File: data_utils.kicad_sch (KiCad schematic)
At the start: 35 parts, among them J10 Conn_01x05, J13 OUTSIDE LED, J5 USB_C_Receptacle_USB2.0_16P, J6 Conn_01x02, J7 Conn_01x02, J8 Conn_01x02, Q4 BC817, Q5 BC817, Q6 BC817, Q7 BC817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

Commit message: near end
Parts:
- R40, R41: footprint Resistor_THT:R_Axial_DIN0309_L9.0mm_D3.2mm_P15.24mm_Horizontal -> Resistor_SMD:R_1210_3225Metric_Pad1.30x2.65mm_HandSolder
- R42: footprint Resistor_THT:R_Axial_DIN0309_L9.0mm_D3.2mm_P15.24mm_Horizontal -> Resistor_SMD:R_0603_1608Metric_Pad0.98x0.95mm_HandSolder
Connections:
- net at R50.2, U8.7 (CANH): now also J6.2 (Pin_2); no longer J6.1 (Pin_1)
- net at R50.1, U8.6 (CANL): now also J6.1 (Pin_1); no longer J6.2 (Pin_2)
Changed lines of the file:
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@@
 	(wire
 		(pts
-			(xy 215.9 121.92) (xy 215.9 129.54)
+			(xy 107.95 48.26) (xy 107.95 44.45)
 		)
 		(stroke
@@
 	(wire
 		(pts
-			(xy 205.74 116.84) (xy 205.74 120.65)
+			(xy 215.9 121.92) (xy 215.9 129.54)
 		)
 		(stroke
@@
 	(wire
 		(pts
-			(xy 107.95 48.26) (xy 107.95 44.45)
+			(xy 205.74 116.84) (xy 205.74 120.65)
 		)
 		(stroke
@@
 			)
 		)
-		(property "Footprint" "Resistor_THT:R_Axial_DIN0309_L9.0mm_D3.2mm_P15.24mm_Horizontal"
+		(property "Footprint" "Resistor_SMD:R_0603_1608Metric_Pad0.98x0.95mm_HandSolder"
 			(at 194.31 57.658 90)
 			(effects
@@
 	(symbol
 		(lib_id "Connector_Generic:Conn_01x02")
-		(at 113.03 48.26 0)
+		(at 113.03 50.8 0)
+		(mirror x)
 		(unit 1)
 		(exclude_from_sim no)
@@
 		(dnp no)
 		(property "Reference" "J6"
-			(at 115.57 48.2599 0)
+			(at 115.57 50.8001 0)
 			(effects
 				(font
@@
 		)
 		(property "Value" "Conn_01x02"
-			(at 109.22 53.848 0)
+			(at 109.22 45.212 0)
 			(effects
 				(font
@@
 		)
 		(property "Footprint" "Connector_PinSocket_2.00mm:PinSocket_1x02_P2.00mm_Horizontal"
-			(at 113.03 48.26 0)
+			(at 113.03 50.8 0)
 			(effects
 				(font
@@
 		)
 		(property "Datasheet" "~"
-			(at 113.03 48.26 0)
+			(at 113.03 50.8 0)
 			(effects
 				(font
@@
 		)
 		(property "Description" "Generic connector, single row, 01x02, script generated (kicad-library-utils/schlib/autogen/connector/)"
-			(at 113.03 48.26 0)
+			(at 113.03 50.8 0)
 			(effects
 				(font
@@
 			)
 		)
-		(property "Footprint" "Resistor_THT:R_Axial_DIN0309_L9.0mm_D3.2mm_P15.24mm_Horizontal"
+		(property "Footprint" "Resistor_SMD:R_1210_3225Metric_Pad1.30x2.65mm_HandSolder"
 			(at 177.8 46.482 90)
 			(effects
@@
 			)
 		)
-		(property "Footprint" "Resistor_THT:R_Axial_DIN0309_L9.0mm_D3.2mm_P15.24mm_Horizontal"
+		(property "Footprint" "Resistor_SMD:R_1210_3225Metric_Pad1.30x2.65mm_HandSolder"
 			(at 177.8 47.498 90)
 			(effects

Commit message: bit artık
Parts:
- R51, R52, R53, R56, R57, R58, R59: footprint Resistor_THT:R_Axial_DIN0207_L6.3mm_D2.5mm_P7.62mm_Horizontal -> Resistor_SMD:R_1210_3225Metric_Pad1.30x2.65mm_HandSolder
- R54, R72: footprint Resistor_SMD:R_0603_1608Metric_Pad0.98x0.95mm_HandSolder -> Resistor_SMD:R_1210_3225Metric_Pad1.30x2.65mm_HandSolder
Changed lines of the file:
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@@
 			)
 		)
-		(property "Footprint" "Resistor_SMD:R_0603_1608Metric_Pad0.98x0.95mm_HandSolder"
+		(property "Footprint" "Resistor_SMD:R_1210_3225Metric_Pad1.30x2.65mm_HandSolder"
 			(at 108.712 107.95 90)
 			(effects
@@
 			)
 		)
-		(property "Footprint" "Resistor_THT:R_Axial_DIN0207_L6.3mm_D2.5mm_P7.62mm_Horizontal"
+		(property "Footprint" "Resistor_SMD:R_1210_3225Metric_Pad1.30x2.65mm_HandSolder"
 			(at 161.29 113.792 90)
 			(effects
@@
 			)
 		)
-		(property "Footprint" "Resistor_THT:R_Axial_DIN0207_L6.3mm_D2.5mm_P7.62mm_Horizontal"
+		(property "Footprint" "Resistor_SMD:R_1210_3225Metric_Pad1.30x2.65mm_HandSolder"
 			(at 67.31 108.712 90)
 			(effects
@@
 			)
 		)
-		(property "Footprint" "Resistor_THT:R_Axial_DIN0207_L6.3mm_D2.5mm_P7.62mm_Horizontal"
+		(property "Footprint" "Resistor_SMD:R_1210_3225Metric_Pad1.30x2.65mm_HandSolder"
 			(at 69.342 118.11 90)
 			(effects
@@
 			)
 		)
-		(property "Footprint" "Resistor_THT:R_Axial_DIN0207_L6.3mm_D2.5mm_P7.62mm_Horizontal"
+		(property "Footprint" "Resistor_SMD:R_1210_3225Metric_Pad1.30x2.65mm_HandSolder"
 			(at 163.322 123.19 90)
 			(effects
@@
 			)
 		)
-		(property "Footprint" "Resistor_THT:R_Axial_DIN0207_L6.3mm_D2.5mm_P7.62mm_Horizontal"
+		(property "Footprint" "Resistor_SMD:R_1210_3225Metric_Pad1.30x2.65mm_HandSolder"
 			(at 102.108 118.11 90)
 			(effects
@@
 			)
 		)
-		(property "Footprint" "Resistor_THT:R_Axial_DIN0207_L6.3mm_D2.5mm_P7.62mm_Horizontal"
+		(property "Footprint" "Resistor_SMD:R_1210_3225Metric_Pad1.30x2.65mm_HandSolder"
 			(at 201.93 115.062 90)
 			(effects
@@
 			)
 		)
-		(property "Footprint" "Resistor_SMD:R_0603_1608Metric_Pad0.98x0.95mm_HandSolder"
+		(property "Footprint" "Resistor_SMD:R_1210_3225Metric_Pad1.30x2.65mm_HandSolder"
 			(at 109.22 95.758 90)
 			(effects
@@
 			)
 		)
-		(property "Footprint" "Resistor_THT:R_Axial_DIN0207_L6.3mm_D2.5mm_P7.62mm_Horizontal"
+		(property "Footprint" "Resistor_SMD:R_1210_3225Metric_Pad1.30x2.65mm_HandSolder"
 			(at 203.962 124.46 90)
 			(effects

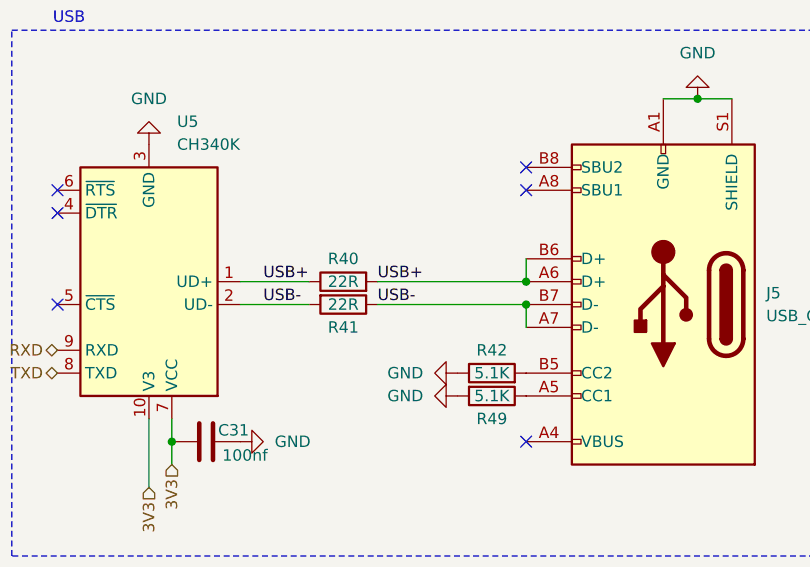
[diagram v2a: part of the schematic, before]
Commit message: esp-32 layout changes
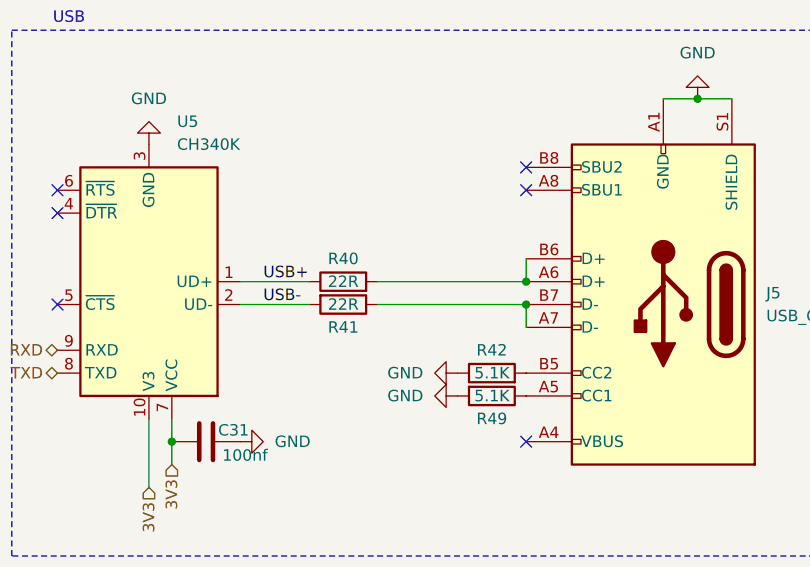
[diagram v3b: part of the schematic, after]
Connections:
- net USB+: no longer J5.A6 (D+), J5.B6 (D+), R40.2
- net USB-: no longer J5.A7 (D-), J5.B7 (D-), R41.1
- new net: J5.A7 (D-), J5.B7 (D-), R41.1
- new net: J5.A6 (D+), J5.B6 (D+), R40.2
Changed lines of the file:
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@@
-	)
-	(label "USB-"
-		(at 181.61 48.26 0)
-		(effects
-			(font
-				(size 1.27 1.27)
-			)
-			(justify left bottom)
-		)
 	)
 	(label "USB-"
@@
 		(effects
 			(font
-				(size 1.27 1.27)
-			)
-			(justify left bottom)
-		)
-	)
-	(label "USB+"
-		(at 181.61 45.72 0)
-		(effects
-			(font

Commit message: BMS DONE IHOPE
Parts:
- removed C31: 100nf, Capacitor_SMD:C_0805_2012Metric_Pad1.18x1.45mm_HandSolder, symbol Device:C
- removed J10: Conn_01x05, Connector_PinSocket_2.00mm:PinSocket_1x05_P2.00mm_Vertical, symbol Connector_Generic:Conn_01x05
- removed R40, R41: 22R, Resistor_SMD:R_1210_3225Metric_Pad1.30x2.65mm_HandSolder, symbol Device:R
- removed U5: CH340K, Package_SO:SSOP-10-1EP_3.9x4.9mm_P1mm_EP2.1x3.3mm, symbol Interface_USB:CH340K
- added J1: Conn_01x09, Connector_PinSocket_2.54mm:PinSocket_1x09_P2.54mm_Vertical, symbol Connector_Generic:Conn_01x09
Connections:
- net +5V: now also J1.9 (Pin_9)
- net GND: now also J1.1 (Pin_1)
- net PB3: now also J1.5 (Pin_5)
- net PB4: now also J1.6 (Pin_6)
- net PB5: now also J1.7 (Pin_7)
- net USB+: now also J5.A6 (D+), J5.B6 (D+)
- net USB-: now also J5.A7 (D-), J5.B7 (D-)
- net at R54.1: now also JP1.1 (A); no longer JP1.3 (B)
- net at R53.1: now also JP1.3 (B); no longer JP1.2 (C)
- net at Q7.2 (E): now also JP1.2 (C); no longer JP1.1 (A)
- new net PB0: J1.2 (Pin_2)
- new net PB1: J1.3 (Pin_3)
- new net PB2: J1.4 (Pin_4)
- new net PB6: J1.8 (Pin_8)
- no-connect marks 6 -> 3
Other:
- moved on the sheet: D6, J13, JP1, R53, R54
